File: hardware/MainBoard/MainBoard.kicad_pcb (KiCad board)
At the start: 2 copper layers, 45 x 80 mm, 29 parts, among them J1 to front board, J2 to front board, J5 Bus 1 power/MIDI, J6 Bus 2 audio, J7 DEBUG UART0, U1 H11L1

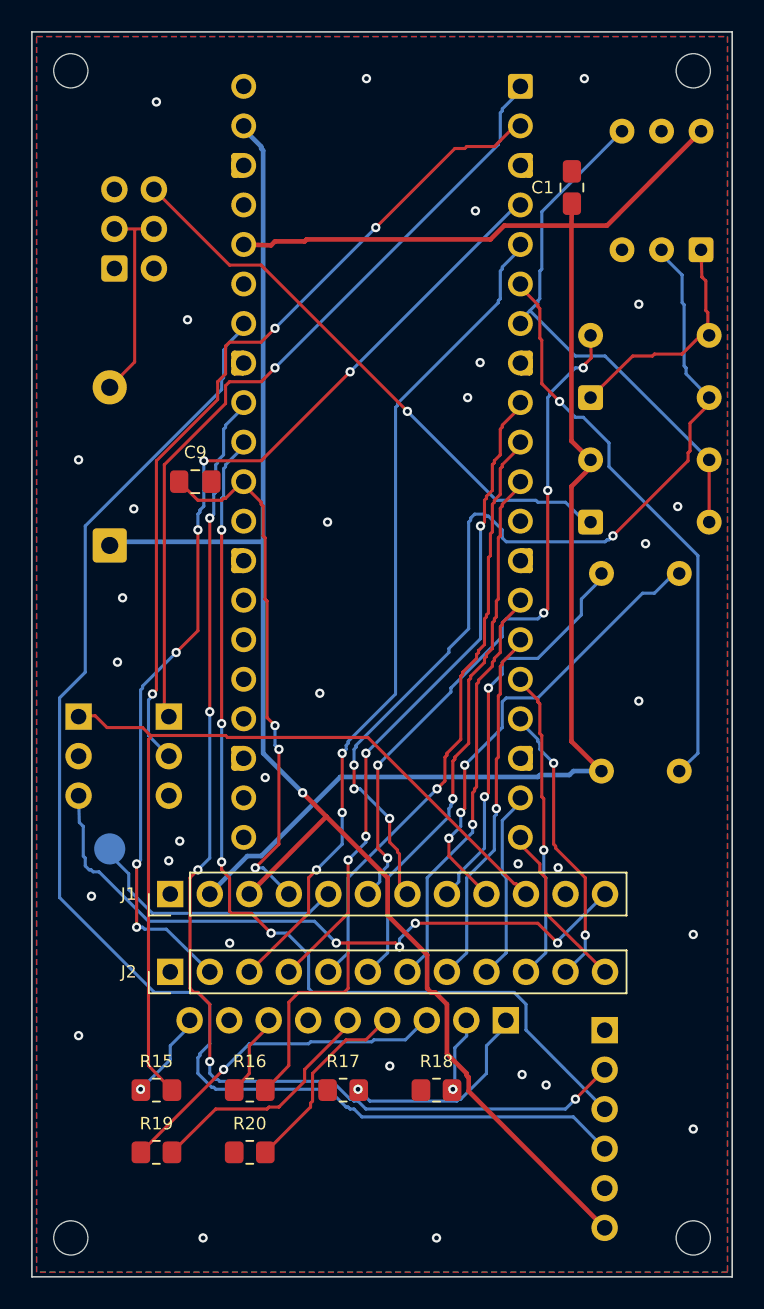
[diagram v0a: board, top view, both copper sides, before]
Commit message: Lay out the front board, where the panel has already decided everything
The main board layout was a series of choices. This one is mostly arithmetic:
the panel fixes where the three encoder shafts, the two buttons and the display
go, and the layout is what falls out. Board origin is panel (2.9, 14), so
SELECT lands at (22.5, 46.58), PARAM A and B at (10.0, 71.61) and (35.0, 71.61),
RUN and BOOT at (7.1, 46.58) and (37.9, 46.58). 229 track segments, 691 mm of
copper, 20 vias, ground poured both sides, DRC clean and in agreement with the
schematic.

What was actually decided:

J3 and J4 sit on the back at exactly the coordinates J1 and J2 occupy on the
main board. That works because both boards are drawn in the same frame -- each
has F.Cu facing the panel -- so a point on one is directly behind the same point
on the other and pin k meets pin k. It is the kind of thing that is obvious
until it is wrong, and wrong means a board that plugs together backwards.

J8 went to the back. On the panel side the encoder bodies fill the entire 6.5 mm
gap, so ten wires have no lane to reach the jacks below; behind the board they
run in the gap between the boards and leave at the bottom edge. For the same
reason its wires are soldered rather than plugged: a 2.54 mm header stands
8.5 mm tall and neither gap has room for one, let alone a housing on top of it.

The pull-ups and debounce footprints sit beside the encoder they serve, on the
back, where the encoders' courtyards do not reach because those are on the other
side of the board.

Both boards' lower standoffs moved from the corners to y 63. At y 77.5 the hole
lands inside the PARAM encoders' courtyards, which is a real DRC error rather
than a cosmetic one, and moving them cost a re-route of the main board -- hence
its board file changing here too. The front board is bolted to the panel by
three encoder nuts regardless.

One thing is not backed by a measurement, and it should be said plainly: DS1 is
drawn centred on the display mo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
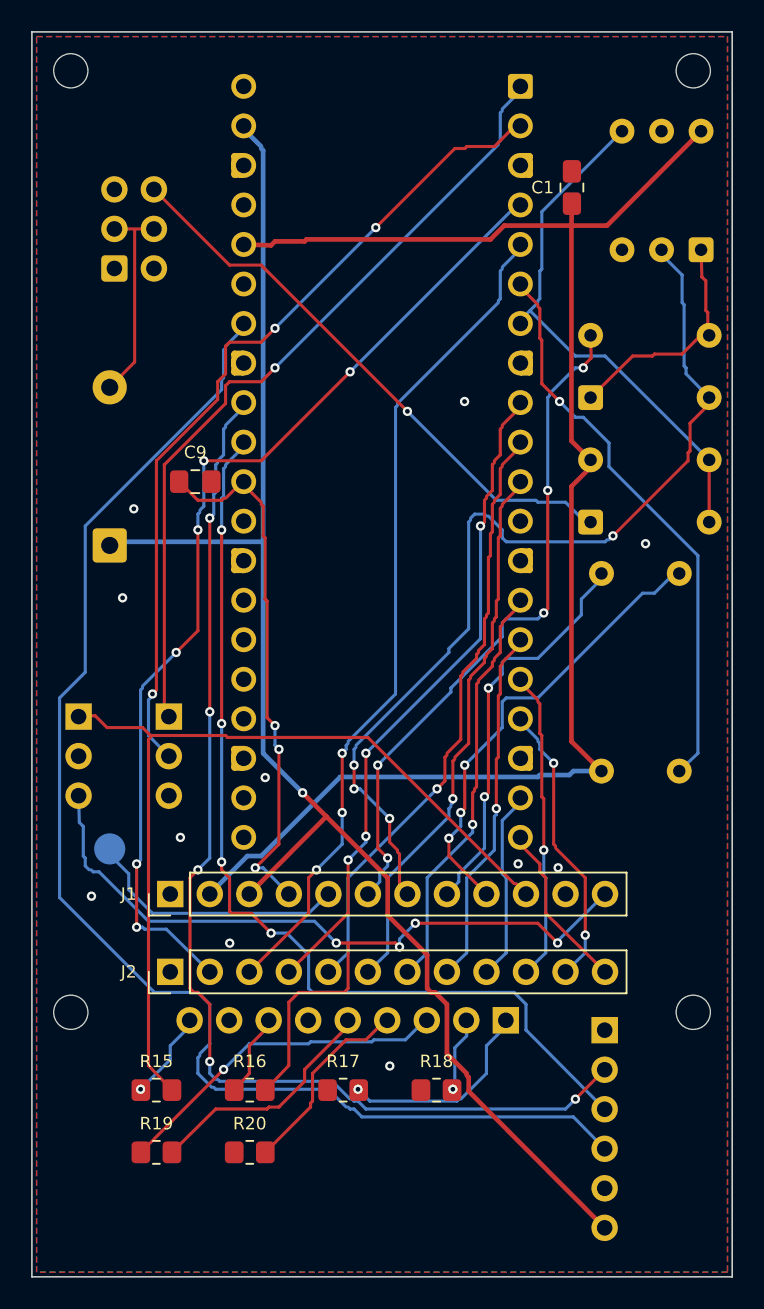
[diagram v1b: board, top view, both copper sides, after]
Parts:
- moved H7 14.5 mm to (2.50, 63.0)
- moved H8 14.5 mm to (42.5, 63.0)
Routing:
- net SEL_DT: track 39.2 -> 38.4 mm
- net SEL_SW: track 35.6 -> 34.8 mm
- net MIDI_IN_5: track 61.5 -> 60.9 mm
- net PA_CLK: track 26.9 -> 26.4 mm
- net SCL: track 54.0 -> 53.5 mm
- net /Main board/I2S_LRCK: track 87.2 -> 86.7 mm
- net /Main board/I2S_BCK: track 72.6 -> 72.1 mm
- net GND: vias 32 -> 11
